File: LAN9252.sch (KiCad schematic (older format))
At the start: 52 parts, among them U1 LAN9252, U2 24LC00, Y1 Crystal_GND24

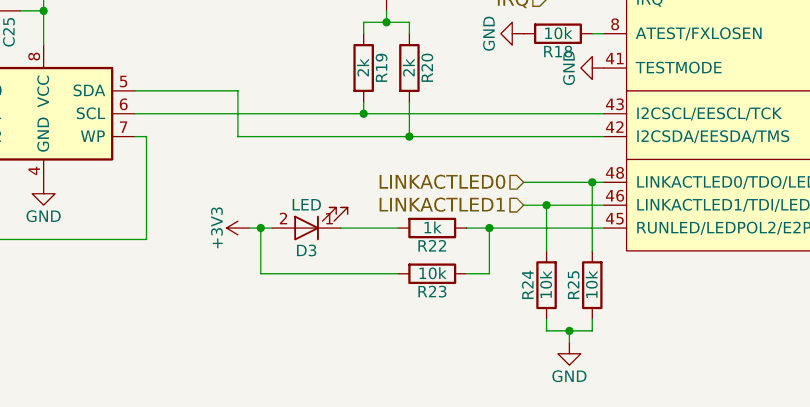
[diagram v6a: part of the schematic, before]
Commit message: LED変更，再アノテーション
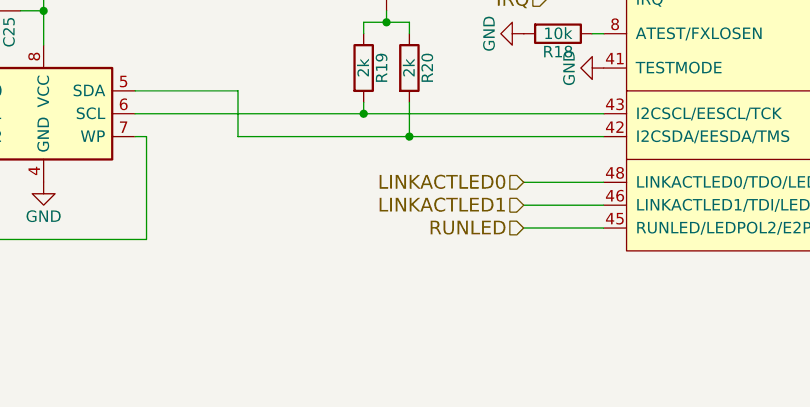
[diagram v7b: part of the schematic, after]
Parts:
- removed D3: LED, LEDs:LED_0603, symbol LED
- removed R22: 1k, Resistors_SMD:R_0603, symbol R
- removed R23, R24, R25: 10k, Resistors_SMD:R_0603, symbol R
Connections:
- net RUNLED: now reaches U1.45 (RUNLED/LEDPOL2/E2PSIZE)
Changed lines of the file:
@@
 $EndDescr
 $Comp
-L GND #PWR021
+L GND #PWR028
 U 1 1 58D8F4AE
 P 6400 6000
-F 0 "#PWR021" H 6400 5750 50  0001 C CNN
+F 0 "#PWR028" H 6400 5750 50  0001 C CNN
 F 1 "GND" H 6400 5850 50  0000 C CNN
 F 2 "" H 6400 6000 50  0000 C CNN
@@
 NoConn ~ 4600 3850
 $Comp
-L GND #PWR022
+L GND #PWR029
 U 1 1 58D8FBF8
 P 4600 4150
-F 0 "#PWR022" H 4600 3900 50  0001 C CNN
+F 0 "#PWR029" H 4600 3900 50  0001 C CNN
 F 1 "GND" H 4600 4000 50  0000 C CNN
 F 2 "" H 4600 4150 50  0000 C CNN
@@
 $EndComp
 $Comp
-L GND #PWR023
+L GND #PWR030
 U 1 1 58D8FC8D
 P 4250 4500
-F 0 "#PWR023" H 4250 4250 50  0001 C CNN
+F 0 "#PWR030" H 4250 4250 50  0001 C CNN
 F 1 "GND" H 4250 4350 50  0000 C CNN
 F 2 "" H 4250 4500 50  0000 C CNN
@@
 $EndComp
 $Comp
-L GND #PWR024
+L GND #PWR031
 U 1 1 58D8FD81
 P 4600 5100
-F 0 "#PWR024" H 4600 4850 50  0001 C CNN
+F 0 "#PWR031" H 4600 4850 50  0001 C CNN
 F 1 "GND" H 4600 4950 50  0000 C CNN
 F 2 "" H 4600 5100 50  0000 C CNN
@@
 $EndComp
 $Comp
-L GND #PWR025
+L GND #PWR032
 U 1 1 58D8CF70
 P 7000 3900
-F 0 "#PWR025" H 7000 3650 50  0001 C CNN
+F 0 "#PWR032" H 7000 3650 50  0001 C CNN
 F 1 "GND" H 7000 3750 50  0000 C CNN
 F 2 "" H 7000 3900 50  0000 C CNN
@@
 $EndComp
 $Comp
-L GND #PWR026
+L GND #PWR033
 U 1 1 58D8D10E
 P 7000 5350
-F 0 "#PWR026" H 7000 5100 50  0001 C CNN
+F 0 "#PWR033" H 7000 5100 50  0001 C CNN
 F 1 "GND" H 7000 5200 50  0000 C CNN
 F 2 "" H 7000 5350 50  0000 C CNN
@@
 $EndComp
 $Comp
-L GND #PWR027
+L GND #PWR034
 U 1 1 58D8D588
 P 8150 4700
-F 0 "#PWR027" H 8150 4450 50  0001 C CNN
+F 0 "#PWR034" H 8150 4450 50  0001 C CNN
 F 1 "GND" H 8150 4550 50  0000 C CNN
 F 2 "" H 8150 4700 50  0000 C CNN
@@
 $EndComp
 $Comp
-L GND #PWR028
+L GND #PWR035
 U 1 1 58D8F32E
 P 9350 5550
-F 0 "#PWR028" H 9350 5300 50  0001 C CNN
+F 0 "#PWR035" H 9350 5300 50  0001 C CNN
 F 1 "GND" H 9350 5400 50  0000 C CNN
 F 2 "" H 9350 5550 50  0000 C CNN
@@
 $EndComp
 $Comp
-L GND #PWR029
+L GND #PWR036
 U 1 1 58DAEFCA
 P 7200 3450
-F 0 "#PWR029" H 7200 3200 50  0001 C CNN
+F 0 "#PWR036" H 7200 3200 50  0001 C CNN
 F 1 "GND" H 7200 3300 50  0000 C CNN
 F 2 "" H 7200 3450 50  0000 C CNN
@@
 $EndComp
 $Comp
-L GND #PWR030
+L GND #PWR037
 U 1 1 58DB2B81
 P 3500 4000
-F 0 "#PWR030" H 3500 3750 50  0001 C CNN
+F 0 "#PWR037" H 3500 3750 50  0001 C CNN
 F 1 "GND" H 3500 3850 50  0000 C CNN
 F 2 "" H 3500 4000 50  0000 C CNN
@@
 $EndComp
 $Comp
-L +3V3 #PWR031
+L +3V3 #PWR038
 U 1 1 58DB404A
 P 3350 1600
-F 0 "#PWR031" H 3350 1450 50  0001 C CNN
+F 0 "#PWR038" H 3350 1450 50  0001 C CNN
 F 1 "+3V3" H 3350 1740 50  0000 C CNN
 F 2 "" H 3350 1600 50  0000 C CNN
@@
 $EndComp
 $Comp
-L GND #PWR032
+L GND #PWR039
 U 1 1 58DBACA0
 P 3400 3000
-F 0 "#PWR032" H 3400 2750 50  0001 C CNN
+F 0 "#PWR039" H 3400 2750 50  0001 C CNN
 F 1 "GND" H 3400 2850 50  0000 C CNN
 F 2 "" H 3400 3000 50  0000 C CNN
@@
 $EndComp
 $Comp
-L +3V3 #PWR033
+L +3V3 #PWR040
 U 1 1 58DBB1A4
 P 5250 3000
-F 0 "#PWR033" H 5250 2850 50  0001 C CNN
+F 0 "#PWR040" H 5250 2850 50  0001 C CNN
 F 1 "+3V3" H 5250 3140 50  0000 C CNN
 F 2 "" H 5250 3000 50  0000 C CNN
@@
 $EndComp
 $Comp
-L +3V3 #PWR034
+L +3V3 #PWR041
 U 1 1 58DBB719
 P 5600 3000
-F 0 "#PWR034" H 5600 2850 50  0001 C CNN
+F 0 "#PWR041" H 5600 2850 50  0001 C CNN
 F 1 "+3V3" H 5600 3140 50  0000 C CNN
 F 2 "" H 5600 3000 50  0000 C CNN
@@
 $EndComp
 $Comp
-L +3V3 #PWR035
+L +3V3 #PWR042
 U 1 1 58DBBE53
 P 4600 4350
-F 0 "#PWR035" H 4600 4200 50  0001 C CNN
+F 0 "#PWR042" H 4600 4200 50  0001 C CNN
 F 1 "+3V3" H 4600 4490 50  0000 C CNN
 F 2 "" H 4600 4350 50  0000 C CNN
@@
 $EndComp
 $Comp
-L GND #PWR036
+L GND #PWR043
 U 1 1 58DBE707
 P 7250 2800
-F 0 "#PWR036" H 7250 2550 50  0001 C CNN
+F 0 "#PWR043" H 7250 2550 50  0001 C CNN
 F 1 "GND" H 7250 2650 50  0000 C CNN
 F 2 "" H 7250 2800 50  0000 C CNN
@@
 $EndComp
 $Comp
-L GND #PWR037
+L GND #PWR044
 U 1 1 58DC454A
 P 2300 2450
-F 0 "#PWR037" H 2300 2200 50  0001 C CNN
+F 0 "#PWR044" H 2300 2200 50  0001 C CNN
 F 1 "GND" H 2300 2300 50  0000 C CNN
 F 2 "" H 2300 2450 50  0000 C CNN
@@
 $EndComp
 $Comp
-L +3V3 #PWR038
+L +3V3 #PWR045
 U 1 1 58DC4AF2
 P 2300 1950
-F 0 "#PWR038" H 2300 1800 50  0001 C CNN
+F 0 "#PWR045" H 2300 1800 50  0001 C CNN
 F 1 "+3V3" H 2300 2090 50  0000 C CNN
 F 2 "" H 2300 1950 50  0000 C CNN
@@
 Text HLabel 4350 4800 0    60   Input ~ 0
 IRQ
-$Comp
-L LED D3
-U 1 1 58DC8FDF
-P 3300 5800
-F 0 "D3" H 3300 5900 50  0000 C CNN
-F 1 "LED" H 3300 5700 50  0000 C CNN
-F 2 "LEDs:LED_0603" H 3300 5800 50  0001 C CNN
-F 3 "" H 3300 5800 50  0000 C CNN
-	1    3300 5800
-	-1   0    0    1
-$EndComp
-$Comp
-L +3V3 #PWR039
-U 1 1 58DC9090
-P 3050 5800
-F 0 "#PWR039" H 3050 5650 50  0001 C CNN
-F 1 "+3V3" H 3050 5940 50  0000 C CNN
-F 2 "" H 3050 5800 50  0000 C CNN
-F 3 "" H 3050 5800 50  0000 C CNN
-	1    3050 5800
-	0    -1   -1   0
-$EndComp
-$Comp
-L R R22
-U 1 1 58DC9456
-P 3850 5800
-F 0 "R22" V 3930 5800 50  0000 C CNN
-F 1 "1k" V 3850 5800 50  0000 C CNN
-F 2 "Resistors_SMD:R_0603" V 3780 5800 50  0001 C CNN
-F 3 "" H 3850 5800 50  0000 C CNN
-	1    3850 5800
-	0    1    1    0
-$EndComp
-$Comp
-L R R23
-U 1 1 58DC9741
-P 3850 6000
-F 0 "R23" V 3930 6000 50  0000 C CNN
-F 1 "10k" V 3850 6000 50  0000 C CNN
-F 2 "Resistors_SMD:R_0603" V 3780 6000 50  0001 C CNN
-F 3 "" H 3850 6000 50  0000 C CNN
-	1    3850 6000
-	0    1    1    0
-$EndComp
-$Comp
-L R R25
-U 1 1 58DCC3A6
-P 4550 6050
-F 0 "R25" V 4630 6050 50  0000 C CNN
-F 1 "10k" V 4550 6050 50  0000 C CNN
-F 2 "Resistors_SMD:R_0603" V 4480 6050 50  0001 C CNN
-F 3 "" H 4550 6050 50  0000 C CNN
-	1    4550 6050
-	-1   0    0    1
-$EndComp
-$Comp
-L R R24
-U 1 1 58DCC474
-P 4350 6050
-F 0 "R24" V 4430 6050 50  0000 C CNN
-F 1 "10k" V 4350 6050 50  0000 C CNN
-F 2 "Resistors_SMD:R_0603" V 4280 6050 50  0001 C CNN
-F 3 "" H 4350 6050 50  0000 C CNN
-	1    4350 6050
-	-1   0    0    1
-$EndComp
-$Comp
-L GND #PWR040
-U 1 1 58DCCAA2
-P 4450 6300
-F 0 "#PWR040" H 4450 6050 50  0001 C CNN
-F 1 "GND" H 4450 6150 50  0000 C CNN
-F 2 "" H 4450 6300 50  0000 C CNN
-F 3 "" H 4450 6300 50  0000 C CNN
-	1    4450 6300
-	1    0    0    -1
-$EndComp
 $Comp
 L R R18
@@
 $EndComp
 $Comp
-L GND #PWR041
+L GND #PWR046
 U 1 1 58DD07AD
 P 4250 4950
-F 0 "#PWR041" H 4250 4700 50  0001 C CNN
+F 0 "#PWR046" H 4250 4700 50  0001 C CNN
 F 1 "GND" H 4250 4800 50  0000 C CNN
 F 2 "" H 4250 4950 50  0000 C CNN
@@
 $EndComp
 $Comp
-L +3V3 #PWR042
+L +3V3 #PWR047
 U 1 1 58DD57EA
 P 3650 4850
-F 0 "#PWR042" H 3650 4700 50  0001 C CNN
+F 0 "#PWR047" H 3650 4700 50  0001 C CNN
 F 1 "+3V3" H 3650 4990 50  0000 C CNN
 F 2 "" H 3650 4850 50  0000 C CNN
@@
 	4600 4800 4350 4800
 Wire Wire Line
-	4000 5800 4600 5800
-Wire Wire Line
-	4000 6000 4100 6000
-Wire Wire Line
-	4100 6000 4100 5800
-Connection ~ 4100 5800
-Wire Wire Line
 	4250 5600 4600 5600
 Wire Wire Line
 	4250 5700 4600 5700
-Wire Wire Line
-	3450 5800 3700 5800
-Wire Wire Line
-	3100 6000 3700 6000
-Wire Wire Line
-	4350 5900 4350 5700
-Connection ~ 4350 5700
-Wire Wire Line
-	4550 5900 4550 5600
-Connection ~ 4550 5600
-Wire Wire Line
-	4350 6200 4350 6250
-Wire Wire Line
-	4350 6250 4550 6250
-Wire Wire Line
-	4550 6250 4550 6200
-Wire Wire Line
-	4450 6300 4450 6250
-Connection ~ 4450 6250
 Wire Wire Line
 	4550 4950 4600 4950
@@
 	3000 5200 3000 5400
 $Comp
-L GND #PWR043
+L GND #PWR048
 U 1 1 58E26D3D
 P 2150 5600
-F 0 "#PWR043" H 2150 5350 50  0001 C CNN
+F 0 "#PWR048" H 2150 5350 50  0001 C CNN
 F 1 "GND" H 2150 5450 50  0000 C CNN
 F 2 "" H 2150 5600 50  0000 C CNN
@@
 Connection ~ 1700 5300
 $Comp
-L GND #PWR044
+L GND #PWR049
 U 1 1 58E27E20
 P 1700 5900
-F 0 "#PWR044" H 1700 5650 50  0001 C CNN
+F 0 "#PWR049" H 1700 5650 50  0001 C CNN
 F 1 "GND" H 1700 5750 50  0000 C CNN
 F 2 "" H 1700 5900 50  0000 C CNN
@@
 $EndComp
 $Comp
-L GND #PWR045
+L GND #PWR050
 U 1 1 58E29423
 P 1750 4850
-F 0 "#PWR045" H 1750 4600 50  0001 C CNN
+F 0 "#PWR050" H 1750 4600 50  0001 C CNN
 F 1 "GND" H 1750 4700 50  0000 C CNN
 F 2 "" H 1750 4850 50  0000 C CNN
@@
 $EndComp
 $Comp
-L +3V3 #PWR046
+L +3V3 #PWR051
 U 1 1 58E2970F
 P 2150 4750
-F 0 "#PWR046" H 2150 4600 50  0001 C CNN
+F 0 "#PWR051" H 2150 4600 50  0001 C CNN
 F 1 "+3V3" H 2150 4890 50  0000 C CNN
 F 2 "" H 2150 4750 50  0000 C CNN
@@
 Connection ~ 6450 3050
 Connection ~ 6800 3350
-Wire Wire Line
-	3100 6000 3100 5800
-Wire Wire Line
-	3050 5800 3150 5800
-Connection ~ 3100 5800
+Text HLabel 4250 5800 0    60   Input ~ 0
+RUNLED
+Wire Wire Line
+	4600 5800 4250 5800
 $EndSCHEMATC

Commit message: GPIOのLED並べた 実質完成
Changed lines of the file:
@@
 $EndDescr
 $Comp
-L GND #PWR028
+L GND #PWR046
 U 1 1 58D8F4AE
 P 6400 6000
-F 0 "#PWR028" H 6400 5750 50  0001 C CNN
+F 0 "#PWR046" H 6400 5750 50  0001 C CNN
 F 1 "GND" H 6400 5850 50  0000 C CNN
 F 2 "" H 6400 6000 50  0000 C CNN
@@
 NoConn ~ 4600 3850
 $Comp
-L GND #PWR029
+L GND #PWR047
 U 1 1 58D8FBF8
 P 4600 4150
-F 0 "#PWR029" H 4600 3900 50  0001 C CNN
+F 0 "#PWR047" H 4600 3900 50  0001 C CNN
 F 1 "GND" H 4600 4000 50  0000 C CNN
 F 2 "" H 4600 4150 50  0000 C CNN
@@
 $EndComp
 $Comp
-L GND #PWR030
+L GND #PWR048
 U 1 1 58D8FC8D
 P 4250 4500
-F 0 "#PWR030" H 4250 4250 50  0001 C CNN
+F 0 "#PWR048" H 4250 4250 50  0001 C CNN
 F 1 "GND" H 4250 4350 50  0000 C CNN
 F 2 "" H 4250 4500 50  0000 C CNN
@@
 $EndComp
 $Comp
-L GND #PWR031
+L GND #PWR049
 U 1 1 58D8FD81
 P 4600 5100
-F 0 "#PWR031" H 4600 4850 50  0001 C CNN
+F 0 "#PWR049" H 4600 4850 50  0001 C CNN
 F 1 "GND" H 4600 4950 50  0000 C CNN
 F 2 "" H 4600 5100 50  0000 C CNN
@@
 $EndComp
 $Comp
-L GND #PWR032
+L GND #PWR050
 U 1 1 58D8CF70
 P 7000 3900
-F 0 "#PWR032" H 7000 3650 50  0001 C CNN
+F 0 "#PWR050" H 7000 3650 50  0001 C CNN
 F 1 "GND" H 7000 3750 50  0000 C CNN
 F 2 "" H 7000 3900 50  0000 C CNN
@@
 $EndComp
 $Comp
-L GND #PWR033
+L GND #PWR051
 U 1 1 58D8D10E
 P 7000 5350
-F 0 "#PWR033" H 7000 5100 50  0001 C CNN
+F 0 "#PWR051" H 7000 5100 50  0001 C CNN
 F 1 "GND" H 7000 5200 50  0000 C CNN
 F 2 "" H 7000 5350 50  0000 C CNN
@@
 $EndComp
 $Comp
-L GND #PWR034
+L GND #PWR052
 U 1 1 58D8D588
 P 8150 4700
-F 0 "#PWR034" H 8150 4450 50  0001 C CNN
+F 0 "#PWR052" H 8150 4450 50  0001 C CNN
 F 1 "GND" H 8150 4550 50  0000 C CNN
 F 2 "" H 8150 4700 50  0000 C CNN
@@
 $EndComp
 $Comp
-L GND #PWR035
+L GND #PWR053
 U 1 1 58D8F32E
 P 9350 5550
-F 0 "#PWR035" H 9350 5300 50  0001 C CNN
+F 0 "#PWR053" H 9350 5300 50  0001 C CNN
 F 1 "GND" H 9350 5400 50  0000 C CNN
 F 2 "" H 9350 5550 50  0000 C CNN
@@
 Text HLabel 9150 4400 2    60   Input ~ 0
 VDDTXRX2
-Text HLabel 4250 5600 0    60   Input ~ 0
+Text HLabel 4350 5600 0    60   Input ~ 0
 LINKACTLED0
-Text HLabel 4250 5700 0    60   Input ~ 0
+Text HLabel 4350 5700 0    60   Input ~ 0
 LINKACTLED1
 $Comp
@@
 $EndComp
 $Comp
-L GND #PWR036
+L GND #PWR054
 U 1 1 58DAEFCA
 P 7200 3450
-F 0 "#PWR036" H 7200 3200 50  0001 C CNN
+F 0 "#PWR054" H 7200 3200 50  0001 C CNN
 F 1 "GND" H 7200 3300 50  0000 C CNN
 F 2 "" H 7200 3450 50  0000 C CNN
@@
 $EndComp
 $Comp
-L GND #PWR037
+L GND #PWR055
 U 1 1 58DB2B81
 P 3500 4000
-F 0 "#PWR037" H 3500 3750 50  0001 C CNN
+F 0 "#PWR055" H 3500 3750 50  0001 C CNN
 F 1 "GND" H 3500 3850 50  0000 C CNN
 F 2 "" H 3500 4000 50  0000 C CNN
@@
 $EndComp
 $Comp
-L +3V3 #PWR038
+L +3V3 #PWR056
 U 1 1 58DB404A
 P 3350 1600
-F 0 "#PWR038" H 3350 1450 50  0001 C CNN
+F 0 "#PWR056" H 3350 1450 50  0001 C CNN
 F 1 "+3V3" H 3350 1740 50  0000 C CNN
 F 2 "" H 3350 1600 50  0000 C CNN
@@
 $EndComp
 $Comp
-L GND #PWR039
+L GND #PWR057
 U 1 1 58DBACA0
 P 3400 3000
-F 0 "#PWR039" H 3400 2750 50  0001 C CNN
+F 0 "#PWR057" H 3400 2750 50  0001 C CNN
 F 1 "GND" H 3400 2850 50  0000 C CNN
 F 2 "" H 3400 3000 50  0000 C CNN
@@
 $EndComp
 $Comp
-L +3V3 #PWR040
+L +3V3 #PWR058
 U 1 1 58DBB1A4
 P 5250 3000
-F 0 "#PWR040" H 5250 2850 50  0001 C CNN
+F 0 "#PWR058" H 5250 2850 50  0001 C CNN
 F 1 "+3V3" H 5250 3140 50  0000 C CNN
 F 2 "" H 5250 3000 50  0000 C CNN
@@
 $EndComp
 $Comp
-L +3V3 #PWR041
+L +3V3 #PWR059
 U 1 1 58DBB719
 P 5600 3000
-F 0 "#PWR041" H 5600 2850 50  0001 C CNN
+F 0 "#PWR059" H 5600 2850 50  0001 C CNN
 F 1 "+3V3" H 5600 3140 50  0000 C CNN
 F 2 "" H 5600 3000 50  0000 C CNN
@@
 $EndComp
 $Comp
-L +3V3 #PWR042
+L +3V3 #PWR060
 U 1 1 58DBBE53
 P 4600 4350
-F 0 "#PWR042" H 4600 4200 50  0001 C CNN
+F 0 "#PWR060" H 4600 4200 50  0001 C CNN
 F 1 "+3V3" H 4600 4490 50  0000 C CNN
 F 2 "" H 4600 4350 50  0000 C CNN
@@
 $EndComp
 $Comp
-L GND #PWR043
+L GND #PWR061
 U 1 1 58DBE707
 P 7250 2800
-F 0 "#PWR043" H 7250 2550 50  0001 C CNN
+F 0 "#PWR061" H 7250 2550 50  0001 C CNN
 F 1 "GND" H 7250 2650 50  0000 C CNN
 F 2 "" H 7250 2800 50  0000 C CNN
@@
 $EndComp
 $Comp
-L GND #PWR044
+L GND #PWR062
 U 1 1 58DC454A
 P 2300 2450
-F 0 "#PWR044" H 2300 2200 50  0001 C CNN
+F 0 "#PWR062" H 2300 2200 50  0001 C CNN
 F 1 "GND" H 2300 2300 50  0000 C CNN
 F 2 "" H 2300 2450 50  0000 C CNN
@@
 $EndComp
 $Comp
-L +3V3 #PWR045
+L +3V3 #PWR063
 U 1 1 58DC4AF2
 P 2300 1950
-F 0 "#PWR045" H 2300 1800 50  0001 C CNN
+F 0 "#PWR063" H 2300 1800 50  0001 C CNN
 F 1 "+3V3" H 2300 2090 50  0000 C CNN
 F 2 "" H 2300 1950 50  0000 C CNN
@@
 $EndComp
 $Comp
-L GND #PWR046
+L GND #PWR064
 U 1 1 58DD07AD
 P 4250 4950
-F 0 "#PWR046" H 4250 4700 50  0001 C CNN
+F 0 "#PWR064" H 4250 4700 50  0001 C CNN
 F 1 "GND" H 4250 4800 50  0000 C CNN
 F 2 "" H 4250 4950 50  0000 C CNN
@@
 $EndComp
 $Comp
-L +3V3 #PWR047
+L +3V3 #PWR065
 U 1 1 58DD57EA
 P 3650 4850
-F 0 "#PWR047" H 3650 4700 50  0001 C CNN
+F 0 "#PWR065" H 3650 4700 50  0001 C CNN
 F 1 "+3V3" H 3650 4990 50  0000 C CNN
 F 2 "" H 3650 4850 50  0000 C CNN
@@
 	4600 4800 4350 4800
 Wire Wire Line
-	4250 5600 4600 5600
-Wire Wire Line
-	4250 5700 4600 5700
+	4350 5600 4600 5600
+Wire Wire Line
+	4350 5700 4600 5700
 Wire Wire Line
 	4550 4950 4600 4950
@@
 	3000 5200 3000 5400
 $Comp
-L GND #PWR048
+L GND #PWR066
 U 1 1 58E26D3D
 P 2150 5600
-F 0 "#PWR048" H 2150 5350 50  0001 C CNN
+F 0 "#PWR066" H 2150 5350 50  0001 C CNN
 F 1 "GND" H 2150 5450 50  0000 C CNN
 F 2 "" H 2150 5600 50  0000 C CNN
@@
 Connection ~ 1700 5300
 $Comp
-L GND #PWR049
+L GND #PWR067
 U 1 1 58E27E20
 P 1700 5900
-F 0 "#PWR049" H 1700 5650 50  0001 C CNN
+F 0 "#PWR067" H 1700 5650 50  0001 C CNN
 F 1 "GND" H 1700 5750 50  0000 C CNN
 F 2 "" H 1700 5900 50  0000 C CNN
@@
 $EndComp
 $Comp
-L GND #PWR050
+L GND #PWR068
 U 1 1 58E29423
 P 1750 4850
-F 0 "#PWR050" H 1750 4600 50  0001 C CNN
+F 0 "#PWR068" H 1750 4600 50  0001 C CNN
 F 1 "GND" H 1750 4700 50  0000 C CNN
 F 2 "" H 1750 4850 50  0000 C CNN
@@
 $EndComp
 $Comp
-L +3V3 #PWR051
+L +3V3 #PWR069
 U 1 1 58E2970F
 P 2150 4750
-F 0 "#PWR051" H 2150 4600 50  0001 C CNN
+F 0 "#PWR069" H 2150 4600 50  0001 C CNN
 F 1 "+3V3" H 2150 4890 50  0000 C CNN
 F 2 "" H 2150 4750 50  0000 C CNN
@@
 Connection ~ 6450 3050
 Connection ~ 6800 3350
-Text HLabel 4250 5800 0    60   Input ~ 0
+Text HLabel 4350 5800 0    60   Input ~ 0
 RUNLED
 Wire Wire Line
-	4600 5800 4250 5800
+	4600 5800 4350 5800
 $EndSCHEMATC
